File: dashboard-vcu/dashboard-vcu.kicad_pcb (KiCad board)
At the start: 2 copper layers, 22 parts, among them IC1 XL1509-5.0E1, J1 776163-1, U1 ATmega2560-16AU, Y1 Resonator

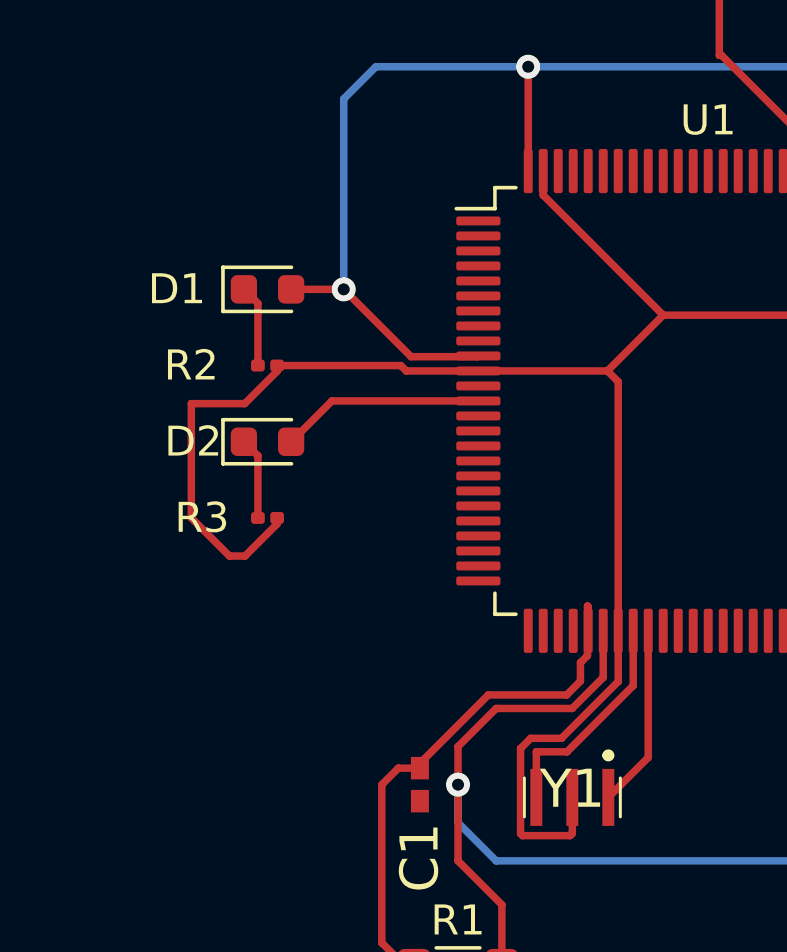
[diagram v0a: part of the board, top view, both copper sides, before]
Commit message: dash tweaks
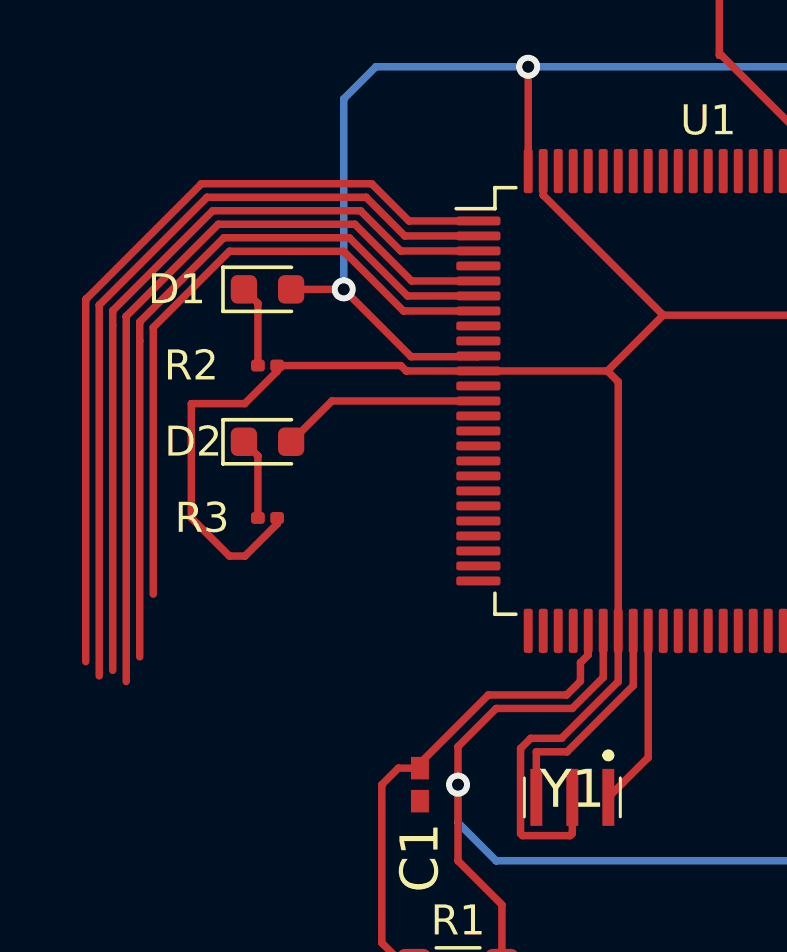
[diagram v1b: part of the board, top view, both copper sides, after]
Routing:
- net PWM4: track 0.00 -> 27.3 mm
- net PWM0: track 0.00 -> 27.0 mm
- net PWM1: track 0.00 -> 26.1 mm
- net PWM5: track 0.00 -> 26.0 mm
- net PWM2: track 0.00 -> 24.4 mm
- net PWM3: track 0.00 -> 21.6 mm
- net RESET: track 18.4 -> 16.7 mm
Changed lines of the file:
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@@
     (thickness 1.6)
     (drawings 0)
-    (tracks 171)
+    (tracks 204)
     (zones 0)
     (modules 22)
@@
   (segment (start 126.8 67.51) (end 127 67.31) (width 0.25) (layer B.Cu) (net 1))
   (segment (start 117.91 67.51) (end 126.8 67.51) (width 0.25) (layer B.Cu) (net 1))
-  (segment (start 119.88501 85.484308) (end 119.88501 87.140692) (width 0.25) (layer F.Cu) (net 2))
-  (segment (start 119.91 85.509298) (end 119.88501 85.484308) (width 0.25) (layer F.Cu) (net 2))
-  (segment (start 119.91 86.3125) (end 119.91 85.509298) (width 0.25) (layer F.Cu) (net 2))
-  (segment (start 119.650692 87.37501) (end 119.650692 87.990078) (width 0.25) (layer F.Cu) (net 2))
-  (segment (start 119.88501 87.140692) (end 119.650692 87.37501) (width 0.25) (layer F.Cu) (net 2))
-  (segment (start 119.650692 87.990078) (end 119.19078 88.44999) (width 0.25) (layer F.Cu) (net 2))
-  (segment (start 119.19078 88.44999) (end 116.580008 88.44999) (width 0.25) (layer F.Cu) (net 2))
-  (segment (start 114.3 90.729998) (end 114.3 90.89) (width 0.25) (layer F.Cu) (net 2))
-  (segment (start 116.580008 88.44999) (end 114.3 90.729998) (width 0.25) (layer F.Cu) (net 2))
   (segment (start 114.3 90.89) (end 113.58 90.89) (width 0.25) (layer F.Cu) (net 2))
   (segment (start 113.58 90.89) (end 113.03 91.44) (width 0.25) (layer F.Cu) (net 2))
   (segment (start 113.03 96.7125) (end 114.1075 97.79) (width 0.25) (layer F.Cu) (net 2))
   (segment (start 113.03 91.44) (end 113.03 96.7125) (width 0.25) (layer F.Cu) (net 2))
+  (segment (start 119.91 87.05) (end 119.91 86.3125) (width 0.25) (layer F.Cu) (net 2))
+  (segment (start 119.91 87.115702) (end 119.91 87.05) (width 0.25) (layer F.Cu) (net 2))
+  (segment (start 119.650692 87.37501) (end 119.91 87.115702) (width 0.25) (layer F.Cu) (net 2))
+  (segment (start 114.3 90.729998) (end 116.580008 88.44999) (width 0.25) (layer F.Cu) (net 2))
+  (segment (start 119.650692 87.990078) (end 119.650692 87.37501) (width 0.25) (layer F.Cu) (net 2))
+  (segment (start 116.580008 88.44999) (end 119.19078 88.44999) (width 0.25) (layer F.Cu) (net 2))
+  (segment (start 119.19078 88.44999) (end 119.650692 87.990078) (width 0.25) (layer F.Cu) (net 2))
+  (segment (start 114.3 90.89) (end 114.3 90.729998) (width 0.25) (layer F.Cu) (net 2))
   (segment (start 140.335 91.255) (end 138.615 91.255) (width 0.25) (layer F.Cu) (net 3))
   (segment (start 138.615 91.255) (end 138.43 91.44) (width 0.25) (layer F.Cu) (net 3))
@@
   (segment (start 111.3675 78.65) (end 116.2475 78.65) (width 0.25) (layer F.Cu) (net 84))
   (segment (start 110.0075 80.01) (end 111.3675 78.65) (width 0.25) (layer F.Cu) (net 84))
+  (segment (start 111.76 73.66) (end 107.95 73.66) (width 0.25) (layer F.Cu) (net 88))
+  (segment (start 113.75 75.65) (end 111.76 73.66) (width 0.25) (layer F.Cu) (net 88))
+  (segment (start 107.95 73.66) (end 105.41 76.2) (width 0.25) (layer F.Cu) (net 88))
+  (segment (start 116.2475 75.65) (end 113.75 75.65) (width 0.25) (layer F.Cu) (net 88))
+  (segment (start 105.41 76.2) (end 105.41 85.09) (width 0.25) (layer F.Cu) (net 88))
+  (segment (start 104.95999 76.0136) (end 104.95999 76.65001) (width 0.25) (layer F.Cu) (net 89))
+  (segment (start 107.763599 73.209991) (end 104.95999 76.0136) (width 0.25) (layer F.Cu) (net 89))
+  (segment (start 111.9464 73.20999) (end 107.763599 73.209991) (width 0.25) (layer F.Cu) (net 89))
+  (segment (start 104.95999 76.65001) (end 104.95999 87.17999) (width 0.25) (layer F.Cu) (net 89))
+  (segment (start 113.88641 75.15) (end 111.9464 73.20999) (width 0.25) (layer F.Cu) (net 89))
+  (segment (start 116.2475 75.15) (end 113.88641 75.15) (width 0.25) (layer F.Cu) (net 89))
+  (segment (start 107.5772 72.75998) (end 104.50998 75.8272) (width 0.25) (layer F.Cu) (net 90))
+  (segment (start 104.50998 75.83002) (end 104.50998 87.99998) (width 0.25) (layer F.Cu) (net 90))
+  (segment (start 112.1328 72.75998) (end 107.5772 72.75998) (width 0.25) (layer F.Cu) (net 90))
+  (segment (start 114.02282 74.65) (end 112.1328 72.75998) (width 0.25) (layer F.Cu) (net 90))
+  (segment (start 104.50998 75.8272) (end 104.50998 75.83002) (width 0.25) (layer F.Cu) (net 90))
+  (segment (start 116.2475 74.65) (end 114.02282 74.65) (width 0.25) (layer F.Cu) (net 90))
+  (segment (start 104.05997 76.11997) (end 104.05997 87.63) (width 0.25) (layer F.Cu) (net 92))
+  (segment (start 104.05997 75.6408) (end 104.05997 76.11997) (width 0.25) (layer F.Cu) (net 92))
+  (segment (start 107.3908 72.30997) (end 104.05997 75.6408) (width 0.25) (layer F.Cu) (net 92))
+  (segment (start 112.3192 72.30997) (end 107.3908 72.30997) (width 0.25) (layer F.Cu) (net 92))
+  (segment (start 113.65923 73.65) (end 112.3192 72.30997) (width 0.25) (layer F.Cu) (net 92))
+  (segment (start 116.2475 73.65) (end 113.65923 73.65) (width 0.25) (layer F.Cu) (net 92))
+  (segment (start 112.5056 71.85996) (end 113.79564 73.15) (width 0.25) (layer F.Cu) (net 93))
+  (segment (start 113.79564 73.15) (end 116.2475 73.15) (width 0.25) (layer F.Cu) (net 93))
+  (segment (start 107.2044 71.85996) (end 112.5056 71.85996) (width 0.25) (layer F.Cu) (net 93))
+  (segment (start 103.609961 75.454399) (end 107.2044 71.85996) (width 0.25) (layer F.Cu) (net 93))
+  (segment (start 103.60996 87.8164) (end 103.609961 75.454399) (width 0.25) (layer F.Cu) (net 93))
+  (segment (start 113.93205 72.65) (end 116.2475 72.65) (width 0.25) (layer F.Cu) (net 94))
+  (segment (start 112.692 71.40995) (end 113.93205 72.65) (width 0.25) (layer F.Cu) (net 94))
+  (segment (start 107.018 71.40995) (end 112.692 71.40995) (width 0.25) (layer F.Cu) (net 94))
+  (segment (start 103.159952 75.268) (end 103.159952 87.340048) (width 0.25) (layer F.Cu) (net 94))
+  (segment (start 103.183975 75.243975) (end 103.159952 75.268) (width 0.25) (layer F.Cu) (net 94))
+  (segment (start 103.183975 75.243975) (end 107.018 71.40995) (width 0.25) (layer F.Cu) (net 94))
   (segment (start 142.875 91.255) (end 142.875 89.535) (width 0.25) (layer F.Cu) (net 95))
   (segment (start 142.875 89.535) (end 147.32 85.09) (width 0.25) (layer F.Cu) (net 95))

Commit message: Tweaks
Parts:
- added IC2: TIP102, Package_TO_SOT_THT:TO270P460X1020X2008-3P, F.Cu at (110.5, 91.4)
- added IC3: TIP102, Package_TO_SOT_THT:TO270P460X1020X2008-3P, F.Cu at (121.9, 91.4)
- added J2: Conn_01x05_MountingPin, Connector_PinHeader_1.00mm:PinHeader_1x05_P1.00mm_Vertical, F.Cu at (110.5, 41.9)
- added R10: 220, Resistor_SMD:R_0201_0603Metric, F.Cu at (133.3, 105.4)
- added R11: 220, Resistor_SMD:R_0201_0603Metric, F.Cu at (130.8, 105.4)
- added R4: 2k2, Resistor_SMD:R_0201_0603Metric, F.Cu at (108.0, 86.4)
- added R5: 2k2, Resistor_SMD:R_0201_0603Metric, F.Cu at (119.4, 86.4)
- added R6: 220, Resistor_SMD:R_0201_0603Metric, F.Cu at (144.8, 105.4)
- added R7: 220, Resistor_SMD:R_0201_0603Metric, F.Cu at (142.2, 105.4)
- added R8: 220, Resistor_SMD:R_0201_0603Metric, F.Cu at (139.7, 105.4)
- added R9: 220, Resistor_SMD:R_0201_0603Metric, F.Cu at (135.9, 105.4)
- moved C1 27.9 mm to (114.3, 63.5), turned to 90 degrees
- moved R1 26.8 mm to (118.1, 71.1)
- moved C11 25.4 mm to (151.1, 54.6)
- moved C2 25.4 mm to (133.3, 54.6)
- moved C3 25.4 mm to (134.6, 54.6)
- moved C4 25.4 mm to (135.9, 54.6)
- moved C6 25.4 mm to (147.3, 68.6)
- moved C7 25.4 mm to (138.4, 54.6)
- moved C8 25.4 mm to (142.2, 54.6)
- moved D1 25.4 mm to (109.2, 49.5)
- moved D2 25.4 mm to (109.2, 54.6)
- moved D4 25.4 mm to (156.2, 54.6)
- moved IC1 25.4 mm to (142.2, 68.6)
- moved U1 25.4 mm to (123.9, 53.2)
- moved C10 25.4 mm to (146.6, 54.5)
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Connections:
- C1 pad 2: Net-(C1-Pad2) -> DTR
- J1 pad 1: Net-(J1-Pad1) -> 12V
- J1 pad 14: Net-(J1-Pad14) -> STATUS_A_R
- J1 pad 15: Net-(J1-Pad15) -> STATUS_A_G
- J1 pad 16: Net-(J1-Pad16) -> STATUS_A_B
- J1 pad 17: Net-(J1-Pad17) -> STATUS_B_R
- J1 pad 18: Net-(J1-Pad18) -> STATUS_B_G
- J1 pad 19: Net-(J1-Pad19) -> STATUS_B_B
- J1 pad 29: 12V -> Net-(J1-Pad29)
- J1 pad 8: Net-(J1-Pad8) -> TEMP_GAUGE
- J1 pad 9: Net-(J1-Pad9) -> FUEL_GAUGE
- U1 pad 2: PWM0 -> RXD0
- U1 pad 3: PWM1 -> TXD0
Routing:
- net GND: track 150.9 -> 346.5 mm
- net 12V: track 56.3 -> 7.18 mm
- net PWM6: track 0.00 -> 46.0 mm, vias 0 -> 1
- net PWM7: track 0.00 -> 43.7 mm, vias 0 -> 1
- net PWM8: track 0.00 -> 39.8 mm, vias 0 -> 1
- net PWM9: track 0.00 -> 38.3 mm, vias 0 -> 1
- net PWM10: track 0.00 -> 35.7 mm, vias 0 -> 1
- net PWM11: track 0.00 -> 34.3 mm, vias 0 -> 1
- net PWM12: track 0.00 -> 31.0 mm, vias 0 -> 1
- net DTR: track 0.00 -> 27.7 mm, vias 0 -> 1
- net PWM0: track 27.0 -> 0.00 mm
- net PWM1: track 26.1 -> 0.00 mm
- net PWM4: track 27.3 -> 47.3 mm, vias 0 -> 1
- net PWM5: track 26.0 -> 45.8 mm, vias 0 -> 1
- net TXD0: track 0.00 -> 19.5 mm
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
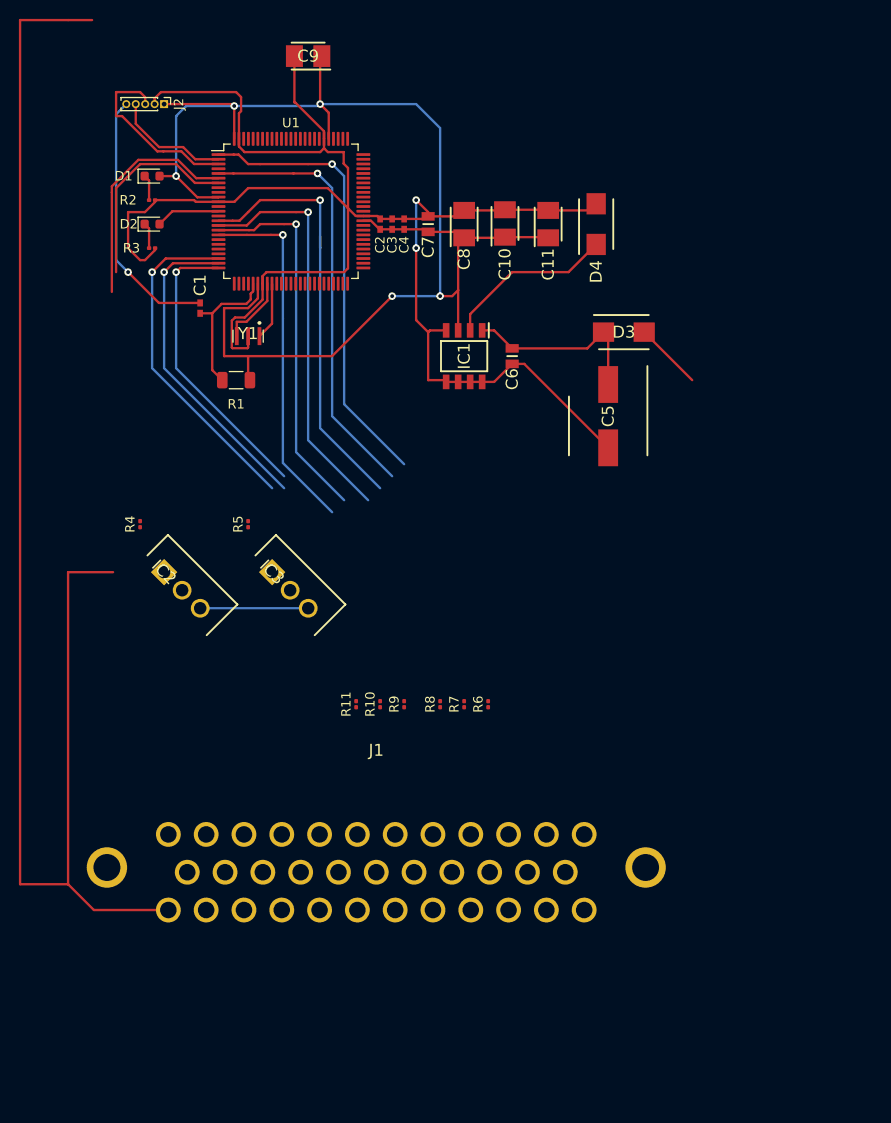
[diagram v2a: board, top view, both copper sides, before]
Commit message: Switch to using Pi Pico for dash vcu
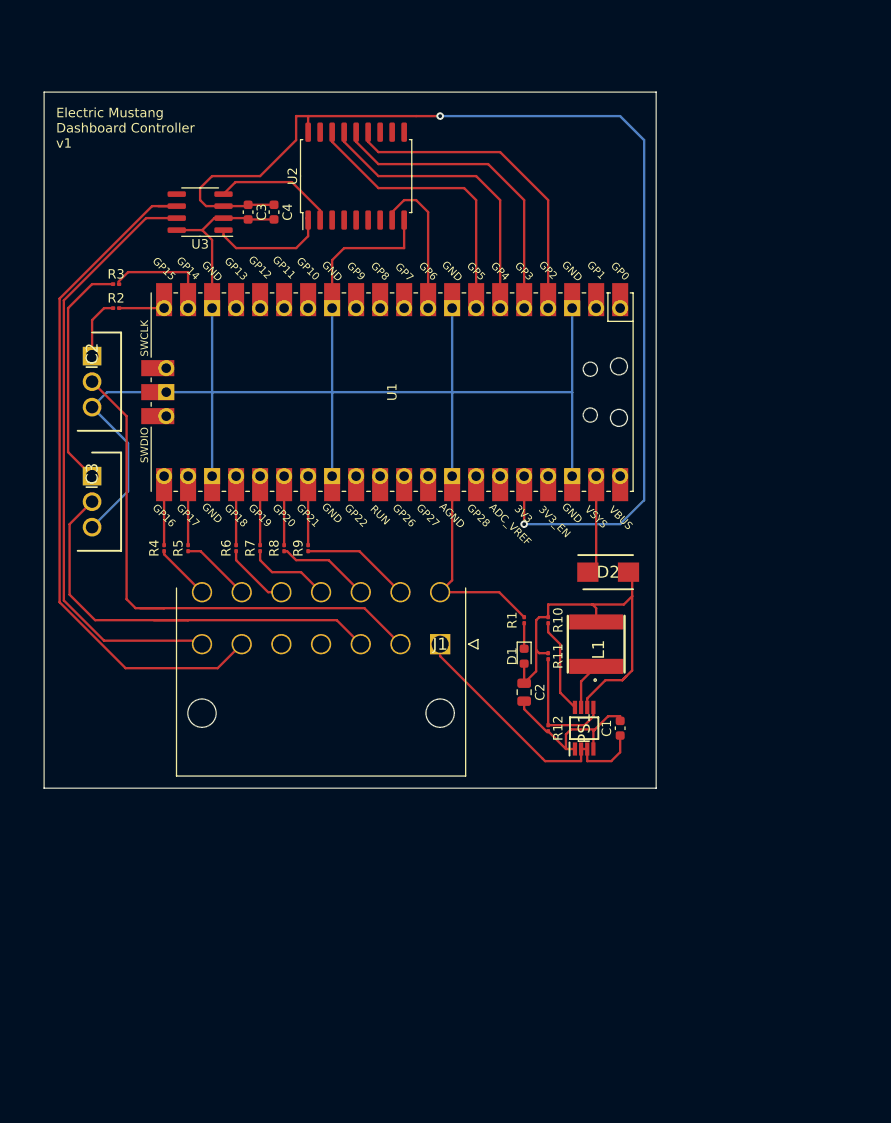
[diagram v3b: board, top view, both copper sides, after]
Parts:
- removed C10, C11, C8, C9: TAJB107K006RNJV, Capacitor_SMD:CAPPM3528X210N
- removed C5: VZH331M1ETT-0810, Capacitor_SMD:CAPAE830X1050N
- removed C6, C7: CL21B105KBFNNNE, Capacitor_SMD:CAPC2012X135N
- removed D3, D4: SS54B, Diode_SMD:DIOM5336X244N
- removed IC1: XL1509-5.0E1, Package_SIP:SOIC127P600X175-8N
- removed J2: Conn_01x05_MountingPin, Connector_PinHeader_1.00mm:PinHeader_1x05_P1.00mm_Vertical
- removed the R2 at (109.2, 52.1)
- removed the R3 at (109.2, 57.1)
- removed Y1: Resonator, RF:CSTNE16M0V530000R0
- added L1: 2.2uH, Inductor_SMD:NR6028T220M, F.Cu at (156.2, 99.1)
- added PS1: TPS62160DGKT, Module:SOP65P490X110-8N, F.Cu at (154.9, 108.0)
- added R10: 100k, Resistor_SMD:R_0201_0603Metric, F.Cu at (151.1, 96.5)
- added R11: 220k, Resistor_SMD:R_0201_0603Metric, F.Cu at (151.1, 100.3)
- added R12: 47k, Resistor_SMD:R_0201_0603Metric, F.Cu at (151.1, 108.0)
- added U2: MCP2515-xSO, Package_SO:SOIC-18W_7.5x11.6mm_P1.27mm, F.Cu at (130.8, 49.5)
- added U3: SN65HVD230, Package_SO:SOIC-8_3.9x4.9mm_P1.27mm, F.Cu at (114.3, 53.3)
- C1: value 0.1uF -> 10uF; footprint Capacitor_SMD:RESC1005X55N -> Capacitor_SMD:C_0603_1608Metric
- C2: value 0.1uF -> 22uF; footprint Capacitor_SMD:RESC1005X55N -> Capacitor_SMD:C_0805_2012Metric
- C3, C4: value 0.1uF -> 100nF; footprint Capacitor_SMD:RESC1005X55N -> Capacitor_SMD:C_0603_1608Metric
- D2: value LED -> SS54B; footprint LED_SMD:LED_0603_1608Metric -> Diode_SMD:DIOM5336X244N
- J1: value 776163-1 -> 39300140; footprint Connector:7761631 -> Connector:39300140
- R1: value 10k -> 1k; footprint Resistor_SMD:R_1206_3216Metric -> Resistor_SMD:R_0201_0603Metric
- U1: value ATmega2560-16AU -> Pico; footprint Package_QFP:TQFP-100_14x14mm_P0.5mm -> Module:RPi_Pico_SMD_TH
- moved D1 64.3 mm to (148.6, 100.3), turned to -90 degrees
- moved C1 62.9 mm to (158.8, 108.0)
- moved D2 60.7 mm to (157.5, 91.4)
- moved C2 51.8 mm to (148.6, 104.1), turned to -90 degrees
- moved R1 39.7 mm to (148.6, 96.5), turned to 90 degrees
- moved R4 38.1 mm to (110.5, 88.9)
- moved R5 33.6 mm to (113.0, 88.9)
- moved J1 32.0 mm to (139.7, 99.1), turned to 0 degrees
- moved R3 29.0 mm to (105.4, 61.0), turned to 0 degrees
- moved R6 27.2 mm to (118.1, 88.9)
- moved IC2 24.1 mm to (102.9, 68.6), turned to -90 degrees
- moved R2 23.0 mm to (105.4, 63.5), turned to 0 degrees
- moved R7 22.5 mm to (120.7, 88.9)
- moved U1 21.9 mm to (134.6, 72.4), turned to -90 degrees
- moved IC3 21.6 mm to (102.9, 81.3), turned to -90 degrees
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- renumbered R4 to R2, R5 to R3, R6 to R4, R7 to R5, R8 to R6, R9 to R7, R10 to R8, R11 to R9
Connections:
- net Net-(U1-Pad14) renamed SPI1_CLK
- C1 pad 1: RESET -> 12V
- C1 pad 2: DTR -> Net-(C1-Pad2)
- C2 pad 2: GND -> Net-(C1-Pad2)
- C3 pad 1: 5V -> 3V
- C4 pad 1: 5V -> 3V
- D2 pad 2: ACT_LED -> 5V
- J1 pad 10: Net-(J1-Pad10) -> STATUS_B_G
- J1 pad 11: Net-(J1-Pad11) -> STATUS_B_R
- J1 pad 12: GND -> STATUS_A_B
- J1 pad 13: Net-(J1-Pad13) -> STATUS_A_G
- J1 pad 2: Net-(J1-Pad2) -> FUEL_GAUGE
- J1 pad 3: Net-(J1-Pad3) -> TEMP_GAUGE
- J1 pad 6: Net-(J1-Pad6) -> CAN_L
- J1 pad 7: Net-(J1-Pad7) -> CAN_H
- J1 pad 8: TEMP_GAUGE -> GND
- J1 pad 9: FUEL_GAUGE -> STATUS_B_B
- R1 pad 1: RESET -> Net-(D1-Pad1)
- R1 pad 2: 5V -> GND
- U1 pad 1: PWM4 -> Net-(U1-Pad1)
- U1 pad 10: 5V -> Net-(U1-Pad10)
- U1 pad 11: GND -> Net-(U1-Pad11)
- U1 pad 13: ACT_LED -> GND
- U1 pad 15: PWM6 -> SPI1_TX
- U1 pad 16: PWM7 -> SPI1_RX
- U1 pad 17: PWM8 -> SPI1_CS
- U1 pad 18: PWM9 -> GND
- U1 pad 19: Net-(U1-Pad19) -> PWM3
- U1 pad 2: RXD0 -> Net-(U1-Pad2)
- U1 pad 20: Net-(U1-Pad20) -> PWM2
- U1 pad 21: Net-(U1-Pad21) -> PWM4
- U1 pad 22: Net-(U1-Pad22) -> PWM5
- U1 pad 23: PWM10 -> GND
- U1 pad 24: PWM11 -> PWM6
- U1 pad 25: PWM12 -> PWM7
- U1 pad 26: PWM13 -> PWM8
- U1 pad 27: Net-(U1-Pad27) -> PWM9
- U1 pad 28: Net-(U1-Pad28) -> GND
- U1 pad 3: TXD0 -> GND
- U1 pad 30: RESET -> Net-(U1-Pad30)
- U1 pad 31: 5V -> Net-(U1-Pad31)
- U1 pad 32: GND -> Net-(U1-Pad32)
- U1 pad 33: XTAL2 -> GND
- U1 pad 34: XTAL1 -> Net-(U1-Pad34)
- U1 pad 36: Net-(U1-Pad36) -> 3V
- U1 pad 38: Net-(U1-Pad38) -> GND
- U1 pad 39: Net-(U1-Pad39) -> Net-(D2-Pad1)
- U1 pad 4: Net-(U1-Pad4) -> SPI0_CLK
- U1 pad 42: Net-(U1-Pad42) -> GND
- U1 pad 5: PWM5 -> SPI0_TX
- U1 pad 6: PWM2 -> SPI0_RX
- U1 pad 7: PWM3 -> SPI0_CS
- U1 pad 8: Net-(U1-Pad8) -> GND
- U1 pad 9: Net-(U1-Pad9) -> 8MHz
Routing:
- net GND: track 346.5 -> 197.0 mm, vias 2 -> 0
- net 3V: track 0.00 -> 120.7 mm, vias 0 -> 2
- net 5V: track 152.4 -> 42.9 mm, vias 5 -> 0
- net CAN_L: track 0.00 -> 73.8 mm
- net CAN_H: track 0.00 -> 63.8 mm
- net FUEL_GAUGE: track 0.00 -> 58.0 mm
- net TEMP_GAUGE: track 0.00 -> 47.5 mm
- net PWM4: track 47.3 -> 7.30 mm, vias 1 -> 0
- net PWM6: track 46.0 -> 7.30 mm, vias 1 -> 0
- net PWM5: track 45.8 -> 7.30 mm, vias 1 -> 0
- net PWM7: track 43.7 -> 7.30 mm, vias 1 -> 0
- net PWM10: track 35.7 -> 0.00 mm, vias 1 -> 0
- net PWM11: track 34.3 -> 0.00 mm, vias 1 -> 0
- net SPI0_CLK: track 0.00 -> 34.1 mm
- net SPI0_TX: track 0.00 -> 32.8 mm
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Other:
- board outline added: 64.8 x 73.7 mm
- net class Default removed
- board text added: "Electric Mustang Dashboard Controller v1"
